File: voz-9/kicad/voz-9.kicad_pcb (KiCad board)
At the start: 2 copper layers, 300 x 140 mm, 189 parts, among them J1 OSC, J2 LFO, J3 DELAY, J4 PATCH A, J5 PATCH B, J6 CTRL, J7 IN+PRE, J8 OUT, J9 EQ424, Q1 J201, Q2 J201, Q3 J201, Q4 J201, Q5 J201, Q6 J201, Q7 2N5457, U1 NE5532, U2 TL072, U3 TL072, U4 MAX1044, U5 78M05, U6 PT2399, U7 PT2399, U8 PT2399, U9 TL072

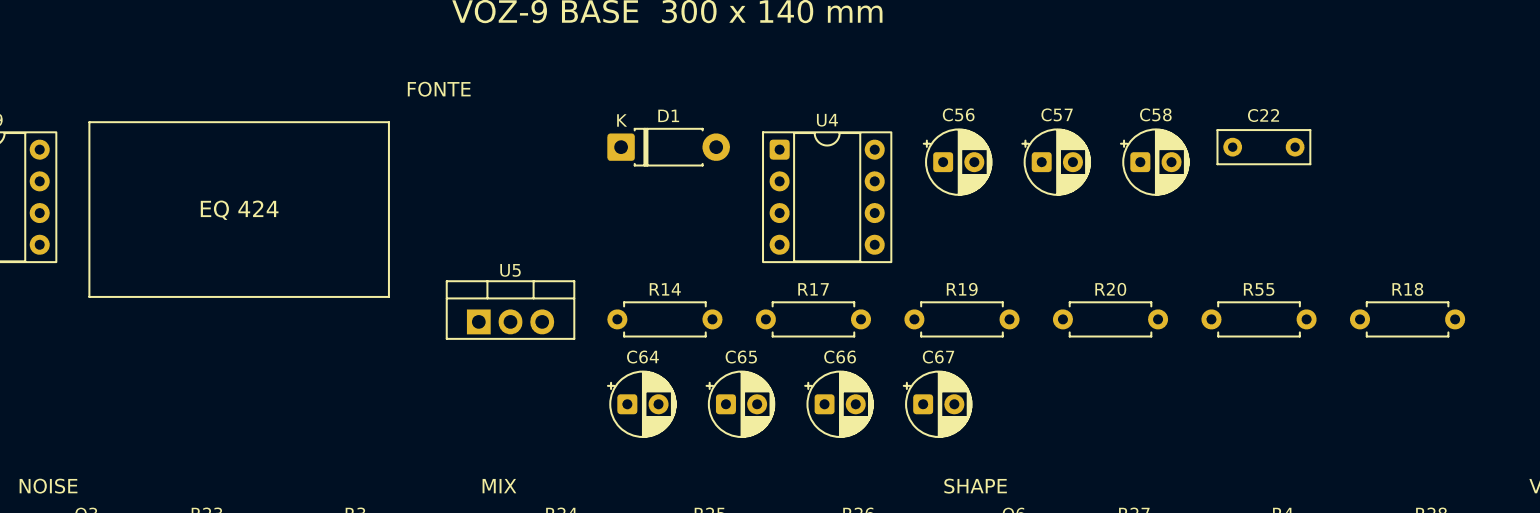
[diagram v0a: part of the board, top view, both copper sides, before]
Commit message: Tira a baía vazia do EQ na seda e encosta a fonte no U9.
O retângulo EQ 424 só reservava espaço em branco ao lado do TL072. A fonte sobe para x=106 mm, sem a caixa na seda.

Co-authored-by: Andrey <andreysenes@users.noreply.github.com>
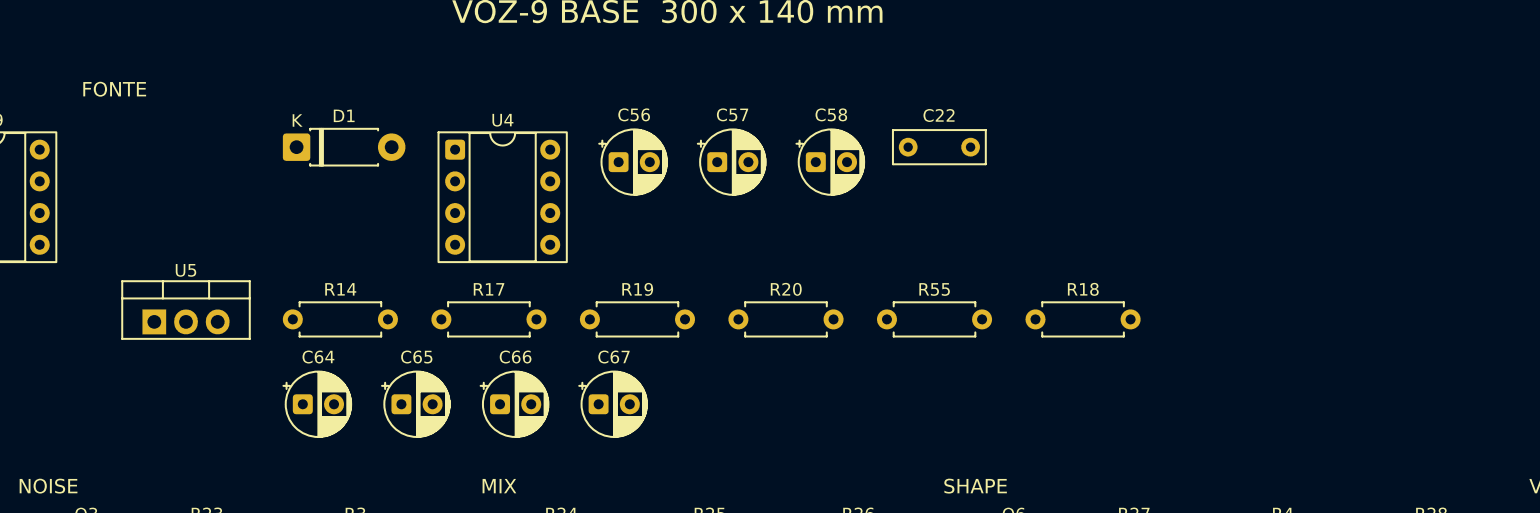
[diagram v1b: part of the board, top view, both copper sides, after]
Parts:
- moved C64 26.0 mm to (120.7, 36.6)
- moved D1 26.0 mm to (120.2, 16.0)
- moved R14 26.0 mm to (119.9, 29.8)
- moved C22 26.0 mm to (169.2, 16.0)
- moved C56 26.0 mm to (146.0, 17.2)
- moved C57 26.0 mm to (153.9, 17.2)
- moved C58 26.0 mm to (161.8, 17.2)
- moved C65 26.0 mm to (128.6, 36.6)
- moved C66 26.0 mm to (136.5, 36.6)
- moved C67 26.0 mm to (144.4, 36.6)
- moved R17 26.0 mm to (131.8, 29.8)
- moved R18 26.0 mm to (179.4, 29.8)
- moved R19 26.0 mm to (143.7, 29.8)
- moved R20 26.0 mm to (155.6, 29.8)
- moved R55 26.0 mm to (167.5, 29.8)
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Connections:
- C1 pad 1: XLR_HOT -> (no net)
- C1 pad 2: GND -> (no net)
- C10 pad 1: U6_LP1 -> (no net)
- C10 pad 2: GND -> (no net)
- C11 pad 1: U7_LP1 -> (no net)
- C11 pad 2: GND -> (no net)
- C12 pad 1: U8_LP1 -> (no net)
- C12 pad 2: GND -> (no net)
- C13 pad 1: U6_OP -> (no net)
- C13 pad 2: U6_OUT -> (no net)
- C14 pad 1: U7_OP -> (no net)
- C14 pad 2: U7_OUT -> (no net)
- C15 pad 1: U8_OP -> (no net)
- C15 pad 2: U8_OUT -> (no net)
- C16 pad 1: U6_LP1 -> (no net)
- C16 pad 2: GND -> (no net)
- C17 pad 1: U7_LP1 -> (no net)
- C17 pad 2: GND -> (no net)
- C18 pad 1: U8_LP1 -> (no net)
- C18 pad 2: GND -> (no net)
- C19 pad 1: V9 -> (no net)
- C19 pad 2: GND -> (no net)
- C2 pad 1: XLR_COLD -> (no net)
- C2 pad 2: GND -> (no net)
- C20 pad 1: U3A_OUT -> (no net)
- C20 pad 2: HEADS -> (no net)
- C21 pad 1: U2A_INM -> (no net)
- C21 pad 2: N4V5 -> (no net)
- C22 pad 1: V5 -> (no net)
- C22 pad 2: GND -> (no net)
- C23 pad 1: V9 -> (no net)
- C23 pad 2: GND -> (no net)
- C24 pad 1: VEE -> (no net)
- C24 pad 2: GND -> (no net)
- C25 pad 1: U1_OA -> (no net)
- C25 pad 2: U1_BP -> (no net)
- C26 pad 1: NOISE_D -> (no net)
- C26 pad 2: NOISE_MIX -> (no net)
- C27 pad 1: PRE_W -> (no net)
- C27 pad 2: FALA -> (no net)
- C28 pad 1: SHAPE -> (no net)
- C28 pad 2: FILT_SW -> (no net)
- C29 pad 1: WET_MIX -> (no net)
- C29 pad 2: LE_IN -> (no net)
- C3 pad 1: WET_LP -> (no net)
- C3 pad 2: GND -> (no net)
- C30 pad 1: MIX -> (no net)
- C30 pad 2: EQ_IN -> (no net)
- C31 pad 1: V5 -> (no net)
- C31 pad 2: GND -> (no net)
- C32 pad 1: V5 -> (no net)
- C32 pad 2: GND -> (no net)
- C33 pad 1: V5 -> (no net)
- C33 pad 2: GND -> (no net)
- C34 pad 1: U6_OUT -> (no net)
- C34 pad 2: U6_SW -> (no net)
- C35 pad 1: U7_OUT -> (no net)
- C35 pad 2: U7_SW -> (no net)
- C36 pad 1: U8_OUT -> (no net)
- C36 pad 2: U8_SW -> (no net)
- C37 pad 1: PT_REF_U6 -> (no net)
- C37 pad 2: GND -> (no net)
- C38 pad 1: PT_REF_U7 -> (no net)
- C38 pad 2: GND -> (no net)
- C39 pad 1: PT_REF_U8 -> (no net)
- C39 pad 2: GND -> (no net)
- C4 pad 1: U3A_IN -> (no net)
- C4 pad 2: U3A_OUT -> (no net)
- C40 pad 1: V9 -> (no net)
- C40 pad 2: GND -> (no net)
- C41 pad 1: PRE_W -> (no net)
- C41 pad 2: OSCIN_CW -> (no net)
- C42 pad 1: U1_OB -> (no net)
- C42 pad 2: PRE_CW -> (no net)
- C43 pad 1: LFO_D -> (no net)
- C43 pad 2: LFO_N1 -> (no net)
- C44 pad 1: LFO_N1 -> (no net)
- C44 pad 2: LFO_N2 -> (no net)
- C45 pad 1: INST_TIP -> (no net)
- C45 pad 2: EXT_IN -> (no net)
- C46 pad 1: TREM_A -> (no net)
- C46 pad 2: LFO_G -> (no net)
- C47 pad 1: VCF -> (no net)
- C47 pad 2: GND -> (no net)
- C48 pad 1: GRAVA_IN -> (no net)
- C48 pad 2: NAB_MID -> (no net)
- C49 pad 1: NAB_BASS -> (no net)
- C49 pad 2: WET -> (no net)
- C5 pad 1: U3B_IN -> (no net)
- C5 pad 2: WET -> (no net)
- C50 pad 1: VCF -> (no net)
- C50 pad 2: VCA_D -> (no net)
- C51 pad 1: U2A_OUT -> (no net)
- C51 pad 2: SW_A -> (no net)
- C52 pad 1: U2B_OUT -> (no net)
- C52 pad 2: SW_B -> (no net)
- C53 pad 1: LFO_D -> (no net)
- C53 pad 2: LFO_AC -> (no net)
- C54 pad 1: VCA_S -> (no net)
- C54 pad 2: DRY -> (no net)
- C55 pad 1: CLK_B -> (no net)
- C55 pad 2: GND -> (no net)
- C56 pad 1: U4_CAP+ -> (no net)
- C56 pad 2: U4_CAP- -> (no net)
- C57 pad 1: VEE -> (no net)
- C57 pad 2: GND -> (no net)
- C58 pad 1: V5 -> (no net)
- C58 pad 2: GND -> (no net)
- C59 pad 1: XLR_HOT -> (no net)
- C59 pad 2: PRE_R12 -> (no net)
- C6 pad 1: U2B_INM -> (no net)
- C6 pad 2: N4V5 -> (no net)
- C60 pad 1: XLR_COLD -> (no net)
- C60 pad 2: PRE_R13 -> (no net)
- C61 pad 1: V9 -> (no net)
- C61 pad 2: GND -> (no net)
- C62 pad 1: VEE -> (no net)
- C62 pad 2: GND -> (no net)
- C63 pad 1: V5 -> (no net)
- C63 pad 2: GND -> (no net)
- C64 pad 1: V9 -> (no net)
- C64 pad 2: GND -> (no net)
- C65 pad 1: VEE -> (no net)
- C65 pad 2: GND -> (no net)
- C66 pad 1: N4V5 -> (no net)
- C66 pad 2: GND -> (no net)
- C67 pad 1: N1V8 -> (no net)
- C67 pad 2: GND -> (no net)
- C68 pad 1: ENV -> (no net)
- C68 pad 2: GND -> (no net)
- C69 pad 1: U7_OUT -> (no net)
- C69 pad 2: U7_SW -> (no net)
- C7 pad 1: U6_CC1 -> (no net)
- C7 pad 2: U6_CC0 -> (no net)
- C70 pad 1: U8_OUT -> (no net)
- C70 pad 2: U8_SW -> (no net)
- C71 pad 1: TREM_B -> (no net)
- C71 pad 2: LFO_G -> (no net)
- C8 pad 1: U7_CC1 -> (no net)
- C8 pad 2: U7_CC0 -> (no net)
- C9 pad 1: U8_CC1 -> (no net)
- C9 pad 2: U8_CC0 -> (no net)
- D1 pad 1: V9 -> (no net)
- D1 pad 2: P4_TIP -> (no net)
- D2 pad 1: ENV -> (no net)
- D2 pad 2: GATE -> (no net)
- D3 pad 1: ENV -> (no net)
- D3 pad 2: FALA_A -> (no net)
- D4 pad 1: CLK_B -> (no net)
- D4 pad 2: CLK_A -> (no net)
- D6 pad 1: GND -> (no net)
- D6 pad 2: SHAPE -> (no net)
- D7 pad 1: GND -> (no net)
- D7 pad 2: WET -> (no net)
- J1 pad 1: OSC_A_POT -> (no net)
- J1 pad 10: GND -> (no net)
- J1 pad 11: N1V8 -> (no net)
- J1 pad 12: CUT_W -> (no net)
- J1 pad 13: GND -> (no net)
- J1 pad 14: SW_A -> (no net)
- J1 pad 15: SW_A_ON -> (no net)
- J1 pad 16: SW_B -> (no net)
- J1 pad 17: SW_B_ON -> (no net)
- J1 pad 18: N1V8 -> (no net)
- J1 pad 19: ENV -> (no net)
- J1 pad 2: U2A_INM -> (no net)
- J1 pad 3: OSC_B_POT -> (no net)
- J1 pad 4: U2B_INM -> (no net)
- J1 pad 5: SUM -> (no net)
- J1 pad 6: AMT_W -> (no net)
- J1 pad 7: GND -> (no net)
- J1 pad 8: EQ_OUT -> (no net)
- J1 pad 9: SHAPE_W -> (no net)
- J2 pad 1: RATE_W -> (no net)
- J2 pad 10: DEPTH_W -> (no net)
- J2 pad 11: PITCH_CV -> (no net)
- J2 pad 12: TIME_CV -> (no net)
- J2 pad 2: RATE_W -> (no net)
- J2 pad 3: GND -> (no net)
- J2 pad 4: LFO_OUT -> (no net)
- J2 pad 5: DEPTH_W -> (no net)
- J2 pad 6: GND -> (no net)
- J2 pad 7: LFO_N2 -> (no net)
- J2 pad 8: TREM_A -> (no net)
- J2 pad 9: TREM_B -> (no net)
- J3 pad 1: V5 -> (no net)
- J3 pad 10: GND -> (no net)
- J3 pad 11: STAR -> (no net)
- J3 pad 12: FB_CW -> (no net)
- J3 pad 13: DRY -> (no net)
- J3 pad 14: WET_W -> (no net)
- J3 pad 15: WET -> (no net)
- J3 pad 16: U6_SW -> (no net)
- J3 pad 17: U7_IN -> (no net)
- J3 pad 18: GND -> (no net)
- J3 pad 19: OUT -> (no net)
- J3 pad 2: TIME_W -> (no net)
- J3 pad 20: WET_W -> (no net)
- J3 pad 3: GND -> (no net)
- J3 pad 4: U6_SW -> (no net)
- J3 pad 5: H1_ON -> (no net)
- J3 pad 6: U7_SW -> (no net)
- J3 pad 7: H2_ON -> (no net)
- J3 pad 8: U8_SW -> (no net)
- J3 pad 9: H3_ON -> (no net)
- J4 pad 1: SW_A_ON -> (no net)
- J4 pad 10: FILT_TIP -> (no net)
- J4 pad 11: FILT_SW -> (no net)
- J4 pad 12: GND -> (no net)
- J4 pad 13: FCV -> (no net)
- J4 pad 15: GND -> (no net)
- J4 pad 16: VCV -> (no net)
- J4 pad 18: GND -> (no net)
- J4 pad 3: GND -> (no net)
- J4 pad 4: SW_B_ON -> (no net)
- J4 pad 6: GND -> (no net)
- J4 pad 7: EXT_IN -> (no net)
- J4 pad 9: GND -> (no net)
- J5 pad 1: LFO_OUT -> (no net)
- J5 pad 10: PRE_W -> (no net)
- J5 pad 12: GND -> (no net)
- J5 pad 13: STAR -> (no net)
- J5 pad 14: PRE_W -> (no net)
- J5 pad 15: GND -> (no net)
- J5 pad 3: GND -> (no net)
- J5 pad 4: TIME_CV -> (no net)
- J5 pad 6: GND -> (no net)
- J5 pad 7: CLK_TIP -> (no net)
- J5 pad 9: GND -> (no net)
- J6 pad 1: LED_A -> (no net)
- J6 pad 2: GND -> (no net)
- J6 pad 3: P4_TIP -> (no net)
- J6 pad 4: GND -> (no net)
- J6 pad 5: GATE -> (no net)
- J6 pad 6: GND -> (no net)
- J7 pad 1: XLR_HOT -> (no net)
- J7 pad 10: MIX -> (no net)
- J7 pad 11: OSCIN_CW -> (no net)
- J7 pad 2: XLR_COLD -> (no net)
- J7 pad 3: GND -> (no net)
- J7 pad 4: INST_TIP -> (no net)
- J7 pad 5: GND -> (no net)
- J7 pad 6: GND -> (no net)
- J7 pad 7: PRE_W -> (no net)
- J7 pad 8: PRE_CW -> (no net)
- J7 pad 9: AMT_W -> (no net)
- J8 pad 1: XLR_OUT -> (no net)
- J8 pad 2: J8_COLD -> (no net)
- J8 pad 3: GND -> (no net)
- J8 pad 4: OUT -> (no net)
- J8 pad 5: GND -> (no net)
- Q1 pad 1: U2A_INM -> (no net)
- Q1 pad 2: Q1G -> (no net)
- Q1 pad 3: N4V5 -> (no net)
- Q2 pad 1: U2B_INM -> (no net)
- Q2 pad 2: Q2G -> (no net)
- Q2 pad 3: N4V5 -> (no net)
- Q3 pad 1: NOISE_D -> (no net)
- Q3 pad 2: Q3G -> (no net)
- Q3 pad 3: NOISE_S -> (no net)
- Q4 pad 1: VCF -> (no net)
- Q4 pad 2: Q4G -> (no net)
- Q4 pad 3: N1V8 -> (no net)
- Q5 pad 1: VCA_D -> (no net)
- Q5 pad 2: ENV -> (no net)
- Q5 pad 3: VCA_S -> (no net)
- Q6 pad 1: V9 -> (no net)
- Q6 pad 2: Q6G -> (no net)
- Q6 pad 3: Q6S -> (no net)
- Q7 pad 1: LFO_D -> (no net)
- Q7 pad 2: LFO_G -> (no net)
- Q7 pad 3: LFO_S -> (no net)
- R1 pad 1: XLR_OUT -> (no net)
- R1 pad 2: GND -> (no net)
- R10 pad 1: H3A -> (no net)
- R10 pad 2: H3B -> (no net)
- R11 pad 1: TIME_W -> (no net)
- R11 pad 2: PT6_U6 -> (no net)
- R12 pad 1: PRE_R12 -> (no net)
- R12 pad 2: U1_INP -> (no net)
- R13 pad 1: PRE_R13 -> (no net)
- R13 pad 2: U1_INM -> (no net)
- R14 pad 1: V9 -> (no net)
- R14 pad 2: LED_A -> (no net)
- R15 pad 1: LFO_G -> (no net)
- R15 pad 2: RATE_W -> (no net)
- R16 pad 1: NAB_MID -> (no net)
- R16 pad 2: U3A_IN -> (no net)
- R18 pad 1: N1V8 -> (no net)
- R18 pad 2: GND -> (no net)
- R19 pad 1: V9 -> (no net)
- R19 pad 2: N4V5 -> (no net)
- R2 pad 1: J8_COLD -> (no net)
- R2 pad 2: GND -> (no net)
- R20 pad 1: N4V5 -> (no net)
- R20 pad 2: GND -> (no net)
- R21 pad 1: U2A_OUT -> (no net)
- R21 pad 2: OSC_A_POT -> (no net)
- R22 pad 1: U2B_OUT -> (no net)
- R22 pad 2: OSC_B_POT -> (no net)
- R23 pad 1: V9 -> (no net)
- R23 pad 2: NOISE_D -> (no net)
- R24 pad 1: SW_A_ON -> (no net)
- R24 pad 2: SUM -> (no net)
- R25 pad 1: SW_B_ON -> (no net)
- R25 pad 2: SUM -> (no net)
- R26 pad 1: EXT_IN -> (no net)
- R26 pad 2: SUM -> (no net)
- R27 pad 1: EQ_OUT -> (no net)
- R27 pad 2: Q6G -> (no net)
- R28 pad 1: Q6S -> (no net)
- R28 pad 2: SHAPE -> (no net)
- R29 pad 1: SHAPE_W -> (no net)
- R29 pad 2: SHAPE -> (no net)
- R3 pad 1: NOISE_S -> (no net)
- R3 pad 2: GND -> (no net)
- R30 pad 1: FILT_TIP -> (no net)
- R30 pad 2: VCF -> (no net)
- R31 pad 1: V9 -> (no net)
- R31 pad 2: LFO_D -> (no net)
- R32 pad 1: LFO_N1 -> (no net)
- R32 pad 2: GND -> (no net)
- R33 pad 1: LFO_N2 -> (no net)
- R33 pad 2: GND -> (no net)
- R34 pad 1: VCA_S -> (no net)
- R34 pad 2: N1V8 -> (no net)
- R35 pad 1: HEADS -> (no net)
- R35 pad 2: U6_IN -> (no net)
- R36 pad 1: HEADS -> (no net)
- R36 pad 2: U7_IN -> (no net)
- R37 pad 1: HEADS -> (no net)
- R37 pad 2: U8_IN -> (no net)
- R38 pad 1: H1_ON -> (no net)
- R38 pad 2: WET_MIX -> (no net)
- R39 pad 1: H2_ON -> (no net)
- R39 pad 2: WET_MIX -> (no net)
- R4 pad 1: Q6S -> (no net)
- R4 pad 2: N4V5 -> (no net)
- R40 pad 1: H3_ON -> (no net)
- R40 pad 2: WET_MIX -> (no net)
- R41 pad 1: U6_IN -> (no net)
- R41 pad 2: U6_LP1 -> (no net)
- R42 pad 1: U1_BM -> (no net)
- R42 pad 2: U1_OB -> (no net)
- R43 pad 1: CLK_A -> (no net)
- R43 pad 2: GND -> (no net)
- R44 pad 1: OUT -> (no net)
- R44 pad 2: XLR_OUT -> (no net)
- R45 pad 1: U3B_IN -> (no net)
- R45 pad 2: NAB_BASS -> (no net)
- R46 pad 1: DRY -> (no net)
- R46 pad 2: STAR -> (no net)
- R47 pad 1: U7_IN -> (no net)
- R47 pad 2: U7_LP1 -> (no net)
- R48 pad 1: U8_IN -> (no net)
- R48 pad 2: U8_LP1 -> (no net)
- R49 pad 1: WET -> (no net)
- R49 pad 2: WET_LP -> (no net)
- R5 pad 1: LFO_S -> (no net)
- R5 pad 2: GND -> (no net)
- R50 pad 1: FALA -> (no net)
- R50 pad 2: FALA_A -> (no net)
- R51 pad 1: STAR -> (no net)
- R51 pad 2: GRAVA_IN -> (no net)
- R52 pad 1: U3A_IN -> (no net)
- R52 pad 2: U3A_OUT -> (no net)
- R53 pad 1: LE_IN -> (no net)
- R53 pad 2: U3B_IN -> (no net)
- R54 pad 1: U3B_IN -> (no net)
- R54 pad 2: WET -> (no net)
- R55 pad 1: V9 -> (no net)
- R55 pad 2: N1V8 -> (no net)
- R56 pad 1: H2B -> (no net)
- R56 pad 2: PT6_U7 -> (no net)
- R57 pad 1: U1_INM -> (no net)
- R57 pad 2: U1_OA -> (no net)
- R58 pad 1: U1_INP -> (no net)
- R58 pad 2: GND -> (no net)
- R59 pad 1: CLK_TIP -> (no net)
- R59 pad 2: CLK_A -> (no net)
- R6 pad 1: U1_BM -> (no net)
- R6 pad 2: GND -> (no net)
- R60 pad 1: H3B -> (no net)
- R60 pad 2: PT6_U8 -> (no net)
- R61 pad 1: VCF -> (no net)
- R61 pad 2: RES_W -> (no net)
- R62 pad 1: U2A_OUT -> (no net)
- R62 pad 2: U2A_INP -> (no net)
- R63 pad 1: U2A_INP -> (no net)
- R63 pad 2: N4V5 -> (no net)
- R64 pad 1: NOISE_MIX -> (no net)
- R64 pad 2: SUM -> (no net)
- R65 pad 1: PITCH_CV -> (no net)
- R65 pad 2: Q1G -> (no net)
- R66 pad 1: PITCH_CV -> (no net)
- R66 pad 2: Q2G -> (no net)
- R67 pad 1: Q4G -> (no net)
- R67 pad 2: FCV -> (no net)
- R68 pad 1: CUT_W -> (no net)
- R68 pad 2: Q4G -> (no net)
- R69 pad 1: ENV -> (no net)
- R69 pad 2: VCV -> (no net)
- R7 pad 1: TIME_W -> (no net)
- R7 pad 2: H2A -> (no net)
- R70 pad 1: CLK_B -> (no net)
- R70 pad 2: TIME_CV -> (no net)
- R71 pad 1: WET -> (no net)
- R71 pad 2: WET_W -> (no net)
- R72 pad 1: U2B_OUT -> (no net)
- R72 pad 2: U2B_INP -> (no net)
- R73 pad 1: U2B_INP -> (no net)
- R73 pad 2: N4V5 -> (no net)
- R74 pad 1: ENV -> (no net)
- R74 pad 2: GND -> (no net)
- R75 pad 1: TIME_CV -> (no net)
- R75 pad 2: PT6_U6 -> (no net)
- R76 pad 1: TIME_CV -> (no net)
- R76 pad 2: PT6_U7 -> (no net)
- R77 pad 1: TIME_CV -> (no net)
- R77 pad 2: PT6_U8 -> (no net)
- R78 pad 1: CLK_B -> (no net)
- R78 pad 2: GND -> (no net)
- R79 pad 1: LFO_AC -> (no net)
- R79 pad 2: LFO_OUT -> (no net)
- R8 pad 1: H2A -> (no net)
- R8 pad 2: H2B -> (no net)
- R80 pad 1: Q3G -> (no net)
- R80 pad 2: GND -> (no net)
- R81 pad 1: LFO_G -> (no net)
- R81 pad 2: GND -> (no net)
- R9 pad 1: TIME_W -> (no net)
- R9 pad 2: H3A -> (no net)
- RV1 pad 1: WET -> (no net)
- RV1 pad 2: FB_CW -> (no net)
- RV1 pad 3: FB_CW -> (no net)
- RV2 pad 1: FILT_TIP -> (no net)
- RV2 pad 2: RES_W -> (no net)
- RV2 pad 3: FILT_TIP -> (no net)
- U1 pad 1: U1_OA -> (no net)
- U1 pad 2: U1_INM -> (no net)
- U1 pad 3: U1_INP -> (no net)
- U1 pad 4: VEE -> (no net)
- U1 pad 5: U1_BP -> (no net)
- U1 pad 6: U1_BM -> (no net)
- U1 pad 7: U1_OB -> (no net)
- U1 pad 8: V9 -> (no net)
- U2 pad 1: U2A_OUT -> (no net)
- U2 pad 2: U2A_INM -> (no net)
- U2 pad 3: U2A_INP -> (no net)
- U2 pad 4: GND -> (no net)
- U2 pad 5: U2B_INP -> (no net)
- U2 pad 6: U2B_INM -> (no net)
- U2 pad 7: U2B_OUT -> (no net)
- U2 pad 8: V9 -> (no net)
- U3 pad 1: U3A_OUT -> (no net)
- U3 pad 2: U3A_IN -> (no net)
- U3 pad 3: GND -> (no net)
- U3 pad 4: VEE -> (no net)
- U3 pad 5: GND -> (no net)
- U3 pad 6: U3B_IN -> (no net)
- U3 pad 7: WET -> (no net)
- U3 pad 8: V9 -> (no net)
- U4 pad 2: U4_CAP+ -> (no net)
- U4 pad 3: GND -> (no net)
- U4 pad 4: U4_CAP- -> (no net)
- U4 pad 5: VEE -> (no net)
- U4 pad 8: V9 -> (no net)
- U5 pad 1: V9 -> (no net)
- U5 pad 2: GND -> (no net)
- U5 pad 3: V5 -> (no net)
- U6 pad 1: V5 -> (no net)
- U6 pad 10: U6_OP -> (no net)
- U6 pad 11: U6_OP -> (no net)
- U6 pad 12: U6_OP -> (no net)
- U6 pad 13: U6_OP -> (no net)
- U6 pad 14: U6_OUT -> (no net)
- U6 pad 15: U6_LP1 -> (no net)
- U6 pad 16: U6_IN -> (no net)
- U6 pad 2: PT_REF_U6 -> (no net)
- U6 pad 3: GND -> (no net)
- U6 pad 4: GND -> (no net)
- U6 pad 6: PT6_U6 -> (no net)
- U6 pad 7: U6_CC1 -> (no net)
- U6 pad 8: U6_CC0 -> (no net)
- U6 pad 9: U6_OP -> (no net)
- U7 pad 1: V5 -> (no net)
- U7 pad 10: U7_OP -> (no net)
- U7 pad 11: U7_OP -> (no net)
- U7 pad 12: U7_OP -> (no net)
- U7 pad 13: U7_OP -> (no net)
- U7 pad 14: U7_OUT -> (no net)
- U7 pad 15: U7_LP1 -> (no net)
- U7 pad 16: U7_IN -> (no net)
- U7 pad 2: PT_REF_U7 -> (no net)
- U7 pad 3: GND -> (no net)
- U7 pad 4: GND -> (no net)
- U7 pad 6: PT6_U7 -> (no net)
- U7 pad 7: U7_CC1 -> (no net)
- U7 pad 8: U7_CC0 -> (no net)
- U7 pad 9: U7_OP -> (no net)
- U8 pad 1: V5 -> (no net)
- U8 pad 10: U8_OP -> (no net)
- U8 pad 11: U8_OP -> (no net)
- U8 pad 12: U8_OP -> (no net)
- U8 pad 13: U8_OP -> (no net)
- U8 pad 14: U8_OUT -> (no net)
- U8 pad 15: U8_LP1 -> (no net)
- U8 pad 16: U8_IN -> (no net)
- U8 pad 2: PT_REF_U8 -> (no net)
- U8 pad 3: GND -> (no net)
- U8 pad 4: GND -> (no net)
- U8 pad 6: PT6_U8 -> (no net)
- U8 pad 7: U8_CC1 -> (no net)
- U8 pad 8: U8_CC0 -> (no net)
- U8 pad 9: U8_OP -> (no net)
- U9 pad 1: EQ_A -> (no net)
- U9 pad 2: EQ_A -> (no net)
- U9 pad 3: EQ_IN -> (no net)
- U9 pad 4: VEE -> (no net)
- U9 pad 5: EQ_A -> (no net)
- U9 pad 6: EQ_OUT -> (no net)
- U9 pad 7: EQ_OUT -> (no net)
- U9 pad 8: V9 -> (no net)
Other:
- board text removed: "EQ 424"

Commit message: Roteia a BASE de 300×140 mm e fecha o H1_ON.
O autorroteador deixou o pino 5 do J3 aberto e dois furos 0,006 mm perto demais. O fechamento agora desvia de pino sem net e de furo, e o DRC fica sem erro e sem pad solto.

Co-authored-by: Andrey <andreysenes@users.noreply.github.com>
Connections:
- C1 pad 1: (no net) -> XLR_HOT
- C1 pad 2: (no net) -> GND
- C10 pad 1: (no net) -> U6_LP1
- C10 pad 2: (no net) -> GND
- C11 pad 1: (no net) -> U7_LP1
- C11 pad 2: (no net) -> GND
- C12 pad 1: (no net) -> U8_LP1
- C12 pad 2: (no net) -> GND
- C13 pad 1: (no net) -> U6_OP
- C13 pad 2: (no net) -> U6_OUT
- C14 pad 1: (no net) -> U7_OP
- C14 pad 2: (no net) -> U7_OUT
- C15 pad 1: (no net) -> U8_OP
- C15 pad 2: (no net) -> U8_OUT
- C16 pad 1: (no net) -> U6_LP1
- C16 pad 2: (no net) -> GND
- C17 pad 1: (no net) -> U7_LP1
- C17 pad 2: (no net) -> GND
- C18 pad 1: (no net) -> U8_LP1
- C18 pad 2: (no net) -> GND
- C19 pad 1: (no net) -> V9
- C19 pad 2: (no net) -> GND
- C2 pad 1: (no net) -> XLR_COLD
- C2 pad 2: (no net) -> GND
- C20 pad 1: (no net) -> U3A_OUT
- C20 pad 2: (no net) -> HEADS
- C21 pad 1: (no net) -> U2A_INM
- C21 pad 2: (no net) -> N4V5
- C22 pad 1: (no net) -> V5
- C22 pad 2: (no net) -> GND
- C23 pad 1: (no net) -> V9
- C23 pad 2: (no net) -> GND
- C24 pad 1: (no net) -> VEE
- C24 pad 2: (no net) -> GND
- C25 pad 1: (no net) -> U1_OA
- C25 pad 2: (no net) -> U1_BP
- C26 pad 1: (no net) -> NOISE_D
- C26 pad 2: (no net) -> NOISE_MIX
- C27 pad 1: (no net) -> PRE_W
- C27 pad 2: (no net) -> FALA
- C28 pad 1: (no net) -> SHAPE
- C28 pad 2: (no net) -> FILT_SW
- C29 pad 1: (no net) -> WET_MIX
- C29 pad 2: (no net) -> LE_IN
- C3 pad 1: (no net) -> WET_LP
- C3 pad 2: (no net) -> GND
- C30 pad 1: (no net) -> MIX
- C30 pad 2: (no net) -> EQ_IN
- C31 pad 1: (no net) -> V5
- C31 pad 2: (no net) -> GND
- C32 pad 1: (no net) -> V5
- C32 pad 2: (no net) -> GND
- C33 pad 1: (no net) -> V5
- C33 pad 2: (no net) -> GND
- C34 pad 1: (no net) -> U6_OUT
- C34 pad 2: (no net) -> U6_SW
- C35 pad 1: (no net) -> U7_OUT
- C35 pad 2: (no net) -> U7_SW
- C36 pad 1: (no net) -> U8_OUT
- C36 pad 2: (no net) -> U8_SW
- C37 pad 1: (no net) -> PT_REF_U6
- C37 pad 2: (no net) -> GND
- C38 pad 1: (no net) -> PT_REF_U7
- C38 pad 2: (no net) -> GND
- C39 pad 1: (no net) -> PT_REF_U8
- C39 pad 2: (no net) -> GND
- C4 pad 1: (no net) -> U3A_IN
- C4 pad 2: (no net) -> U3A_OUT
- C40 pad 1: (no net) -> V9
- C40 pad 2: (no net) -> GND
- C41 pad 1: (no net) -> PRE_W
- C41 pad 2: (no net) -> OSCIN_CW
- C42 pad 1: (no net) -> U1_OB
- C42 pad 2: (no net) -> PRE_CW
- C43 pad 1: (no net) -> LFO_D
- C43 pad 2: (no net) -> LFO_N1
- C44 pad 1: (no net) -> LFO_N1
- C44 pad 2: (no net) -> LFO_N2
- C45 pad 1: (no net) -> INST_TIP
- C45 pad 2: (no net) -> EXT_IN
- C46 pad 1: (no net) -> TREM_A
- C46 pad 2: (no net) -> LFO_G
- C47 pad 1: (no net) -> VCF
- C47 pad 2: (no net) -> GND
- C48 pad 1: (no net) -> GRAVA_IN
- C48 pad 2: (no net) -> NAB_MID
- C49 pad 1: (no net) -> NAB_BASS
- C49 pad 2: (no net) -> WET
- C5 pad 1: (no net) -> U3B_IN
- C5 pad 2: (no net) -> WET
- C50 pad 1: (no net) -> VCF
- C50 pad 2: (no net) -> VCA_D
- C51 pad 1: (no net) -> U2A_OUT
- C51 pad 2: (no net) -> SW_A
- C52 pad 1: (no net) -> U2B_OUT
- C52 pad 2: (no net) -> SW_B
- C53 pad 1: (no net) -> LFO_D
- C53 pad 2: (no net) -> LFO_AC
- C54 pad 1: (no net) -> VCA_S
- C54 pad 2: (no net) -> DRY
- C55 pad 1: (no net) -> CLK_B
- C55 pad 2: (no net) -> GND
- C56 pad 1: (no net) -> U4_CAP+
- C56 pad 2: (no net) -> U4_CAP-
- C57 pad 1: (no net) -> VEE
- C57 pad 2: (no net) -> GND
- C58 pad 1: (no net) -> V5
- C58 pad 2: (no net) -> GND
- C59 pad 1: (no net) -> XLR_HOT
- C59 pad 2: (no net) -> PRE_R12
- C6 pad 1: (no net) -> U2B_INM
- C6 pad 2: (no net) -> N4V5
- C60 pad 1: (no net) -> XLR_COLD
- C60 pad 2: (no net) -> PRE_R13
- C61 pad 1: (no net) -> V9
- C61 pad 2: (no net) -> GND
- C62 pad 1: (no net) -> VEE
- C62 pad 2: (no net) -> GND
- C63 pad 1: (no net) -> V5
- C63 pad 2: (no net) -> GND
- C64 pad 1: (no net) -> V9
- C64 pad 2: (no net) -> GND
- C65 pad 1: (no net) -> VEE
- C65 pad 2: (no net) -> GND
- C66 pad 1: (no net) -> N4V5
- C66 pad 2: (no net) -> GND
- C67 pad 1: (no net) -> N1V8
- C67 pad 2: (no net) -> GND
- C68 pad 1: (no net) -> ENV
- C68 pad 2: (no net) -> GND
- C69 pad 1: (no net) -> U7_OUT
- C69 pad 2: (no net) -> U7_SW
- C7 pad 1: (no net) -> U6_CC1
- C7 pad 2: (no net) -> U6_CC0
- C70 pad 1: (no net) -> U8_OUT
- C70 pad 2: (no net) -> U8_SW
- C71 pad 1: (no net) -> TREM_B
- C71 pad 2: (no net) -> LFO_G
- C8 pad 1: (no net) -> U7_CC1
- C8 pad 2: (no net) -> U7_CC0
- C9 pad 1: (no net) -> U8_CC1
- C9 pad 2: (no net) -> U8_CC0
- D1 pad 1: (no net) -> V9
- D1 pad 2: (no net) -> P4_TIP
- D2 pad 1: (no net) -> ENV
- D2 pad 2: (no net) -> GATE
- D3 pad 1: (no net) -> ENV
- D3 pad 2: (no net) -> FALA_A
- D4 pad 1: (no net) -> CLK_B
- D4 pad 2: (no net) -> CLK_A
- D6 pad 1: (no net) -> GND
- D6 pad 2: (no net) -> SHAPE
- D7 pad 1: (no net) -> GND
- D7 pad 2: (no net) -> WET
- J1 pad 1: (no net) -> OSC_A_POT
- J1 pad 10: (no net) -> GND
- J1 pad 11: (no net) -> N1V8
- J1 pad 12: (no net) -> CUT_W
- J1 pad 13: (no net) -> GND
- J1 pad 14: (no net) -> SW_A
- J1 pad 15: (no net) -> SW_A_ON
- J1 pad 16: (no net) -> SW_B
- J1 pad 17: (no net) -> SW_B_ON
- J1 pad 18: (no net) -> N1V8
- J1 pad 19: (no net) -> ENV
- J1 pad 2: (no net) -> U2A_INM
- J1 pad 3: (no net) -> OSC_B_POT
- J1 pad 4: (no net) -> U2B_INM
- J1 pad 5: (no net) -> SUM
- J1 pad 6: (no net) -> AMT_W
- J1 pad 7: (no net) -> GND
- J1 pad 8: (no net) -> EQ_OUT
- J1 pad 9: (no net) -> SHAPE_W
- J2 pad 1: (no net) -> RATE_W
- J2 pad 10: (no net) -> DEPTH_W
- J2 pad 11: (no net) -> PITCH_CV
- J2 pad 12: (no net) -> TIME_CV
- J2 pad 2: (no net) -> RATE_W
- J2 pad 3: (no net) -> GND
- J2 pad 4: (no net) -> LFO_OUT
- J2 pad 5: (no net) -> DEPTH_W
- J2 pad 6: (no net) -> GND
- J2 pad 7: (no net) -> LFO_N2
- J2 pad 8: (no net) -> TREM_A
- J2 pad 9: (no net) -> TREM_B
- J3 pad 1: (no net) -> V5
- J3 pad 10: (no net) -> GND
- J3 pad 11: (no net) -> STAR
- J3 pad 12: (no net) -> FB_CW
- J3 pad 13: (no net) -> DRY
- J3 pad 14: (no net) -> WET_W
- J3 pad 15: (no net) -> WET
- J3 pad 16: (no net) -> U6_SW
- J3 pad 17: (no net) -> U7_IN
- J3 pad 18: (no net) -> GND
- J3 pad 19: (no net) -> OUT
- J3 pad 2: (no net) -> TIME_W
- J3 pad 20: (no net) -> WET_W
- J3 pad 3: (no net) -> GND
- J3 pad 4: (no net) -> U6_SW
- J3 pad 5: (no net) -> H1_ON
- J3 pad 6: (no net) -> U7_SW
- J3 pad 7: (no net) -> H2_ON
- J3 pad 8: (no net) -> U8_SW
- J3 pad 9: (no net) -> H3_ON
- J4 pad 1: (no net) -> SW_A_ON
- J4 pad 10: (no net) -> FILT_TIP
- J4 pad 11: (no net) -> FILT_SW
- J4 pad 12: (no net) -> GND
- J4 pad 13: (no net) -> FCV
- J4 pad 15: (no net) -> GND
- J4 pad 16: (no net) -> VCV
- J4 pad 18: (no net) -> GND
- J4 pad 3: (no net) -> GND
- J4 pad 4: (no net) -> SW_B_ON
- J4 pad 6: (no net) -> GND
- J4 pad 7: (no net) -> EXT_IN
- J4 pad 9: (no net) -> GND
- J5 pad 1: (no net) -> LFO_OUT
- J5 pad 10: (no net) -> PRE_W
- J5 pad 12: (no net) -> GND
- J5 pad 13: (no net) -> STAR
- J5 pad 14: (no net) -> PRE_W
- J5 pad 15: (no net) -> GND
- J5 pad 3: (no net) -> GND
- J5 pad 4: (no net) -> TIME_CV
- J5 pad 6: (no net) -> GND
- J5 pad 7: (no net) -> CLK_TIP
- J5 pad 9: (no net) -> GND
- J6 pad 1: (no net) -> LED_A
- J6 pad 2: (no net) -> GND
- J6 pad 3: (no net) -> P4_TIP
- J6 pad 4: (no net) -> GND
- J6 pad 5: (no net) -> GATE
- J6 pad 6: (no net) -> GND
- J7 pad 1: (no net) -> XLR_HOT
- J7 pad 10: (no net) -> MIX
- J7 pad 11: (no net) -> OSCIN_CW
- J7 pad 2: (no net) -> XLR_COLD
- J7 pad 3: (no net) -> GND
- J7 pad 4: (no net) -> INST_TIP
- J7 pad 5: (no net) -> GND
- J7 pad 6: (no net) -> GND
- J7 pad 7: (no net) -> PRE_W
- J7 pad 8: (no net) -> PRE_CW
- J7 pad 9: (no net) -> AMT_W
- J8 pad 1: (no net) -> XLR_OUT
- J8 pad 2: (no net) -> J8_COLD
- J8 pad 3: (no net) -> GND
- J8 pad 4: (no net) -> OUT
- J8 pad 5: (no net) -> GND
- Q1 pad 1: (no net) -> U2A_INM
- Q1 pad 2: (no net) -> Q1G
- Q1 pad 3: (no net) -> N4V5
- Q2 pad 1: (no net) -> U2B_INM
- Q2 pad 2: (no net) -> Q2G
- Q2 pad 3: (no net) -> N4V5
- Q3 pad 1: (no net) -> NOISE_D
- Q3 pad 2: (no net) -> Q3G
- Q3 pad 3: (no net) -> NOISE_S
- Q4 pad 1: (no net) -> VCF
- Q4 pad 2: (no net) -> Q4G
- Q4 pad 3: (no net) -> N1V8
- Q5 pad 1: (no net) -> VCA_D
- Q5 pad 2: (no net) -> ENV
- Q5 pad 3: (no net) -> VCA_S
- Q6 pad 1: (no net) -> V9
- Q6 pad 2: (no net) -> Q6G
- Q6 pad 3: (no net) -> Q6S
- Q7 pad 1: (no net) -> LFO_D
- Q7 pad 2: (no net) -> LFO_G
- Q7 pad 3: (no net) -> LFO_S
- R1 pad 1: (no net) -> XLR_OUT
- R1 pad 2: (no net) -> GND
- R10 pad 1: (no net) -> H3A
- R10 pad 2: (no net) -> H3B
- R11 pad 1: (no net) -> TIME_W
- R11 pad 2: (no net) -> PT6_U6
- R12 pad 1: (no net) -> PRE_R12
- R12 pad 2: (no net) -> U1_INP
- R13 pad 1: (no net) -> PRE_R13
- R13 pad 2: (no net) -> U1_INM
- R14 pad 1: (no net) -> V9
- R14 pad 2: (no net) -> LED_A
- R15 pad 1: (no net) -> LFO_G
- R15 pad 2: (no net) -> RATE_W
- R16 pad 1: (no net) -> NAB_MID
- R16 pad 2: (no net) -> U3A_IN
- R18 pad 1: (no net) -> N1V8
- R18 pad 2: (no net) -> GND
- R19 pad 1: (no net) -> V9
- R19 pad 2: (no net) -> N4V5
- R2 pad 1: (no net) -> J8_COLD
- R2 pad 2: (no net) -> GND
- R20 pad 1: (no net) -> N4V5
- R20 pad 2: (no net) -> GND
- R21 pad 1: (no net) -> U2A_OUT
- R21 pad 2: (no net) -> OSC_A_POT
- R22 pad 1: (no net) -> U2B_OUT
- R22 pad 2: (no net) -> OSC_B_POT
- R23 pad 1: (no net) -> V9
- R23 pad 2: (no net) -> NOISE_D
- R24 pad 1: (no net) -> SW_A_ON
- R24 pad 2: (no net) -> SUM
- R25 pad 1: (no net) -> SW_B_ON
- R25 pad 2: (no net) -> SUM
- R26 pad 1: (no net) -> EXT_IN
- R26 pad 2: (no net) -> SUM
- R27 pad 1: (no net) -> EQ_OUT
- R27 pad 2: (no net) -> Q6G
- R28 pad 1: (no net) -> Q6S
- R28 pad 2: (no net) -> SHAPE
- R29 pad 1: (no net) -> SHAPE_W
- R29 pad 2: (no net) -> SHAPE
- R3 pad 1: (no net) -> NOISE_S
- R3 pad 2: (no net) -> GND
- R30 pad 1: (no net) -> FILT_TIP
- R30 pad 2: (no net) -> VCF
- R31 pad 1: (no net) -> V9
- R31 pad 2: (no net) -> LFO_D
- R32 pad 1: (no net) -> LFO_N1
- R32 pad 2: (no net) -> GND
- R33 pad 1: (no net) -> LFO_N2
- R33 pad 2: (no net) -> GND
- R34 pad 1: (no net) -> VCA_S
- R34 pad 2: (no net) -> N1V8
- R35 pad 1: (no net) -> HEADS
- R35 pad 2: (no net) -> U6_IN
- R36 pad 1: (no net) -> HEADS
- R36 pad 2: (no net) -> U7_IN
- R37 pad 1: (no net) -> HEADS
- R37 pad 2: (no net) -> U8_IN
- R38 pad 1: (no net) -> H1_ON
- R38 pad 2: (no net) -> WET_MIX
- R39 pad 1: (no net) -> H2_ON
- R39 pad 2: (no net) -> WET_MIX
- R4 pad 1: (no net) -> Q6S
- R4 pad 2: (no net) -> N4V5
- R40 pad 1: (no net) -> H3_ON
- R40 pad 2: (no net) -> WET_MIX
- R41 pad 1: (no net) -> U6_IN
- R41 pad 2: (no net) -> U6_LP1
- R42 pad 1: (no net) -> U1_BM
- R42 pad 2: (no net) -> U1_OB
- R43 pad 1: (no net) -> CLK_A
- R43 pad 2: (no net) -> GND
- R44 pad 1: (no net) -> OUT
- R44 pad 2: (no net) -> XLR_OUT
- R45 pad 1: (no net) -> U3B_IN
- R45 pad 2: (no net) -> NAB_BASS
- R46 pad 1: (no net) -> DRY
- R46 pad 2: (no net) -> STAR
- R47 pad 1: (no net) -> U7_IN
- R47 pad 2: (no net) -> U7_LP1
- R48 pad 1: (no net) -> U8_IN
- R48 pad 2: (no net) -> U8_LP1
- R49 pad 1: (no net) -> WET
- R49 pad 2: (no net) -> WET_LP
- R5 pad 1: (no net) -> LFO_S
- R5 pad 2: (no net) -> GND
- R50 pad 1: (no net) -> FALA
- R50 pad 2: (no net) -> FALA_A
- R51 pad 1: (no net) -> STAR
- R51 pad 2: (no net) -> GRAVA_IN
- R52 pad 1: (no net) -> U3A_IN
- R52 pad 2: (no net) -> U3A_OUT
- R53 pad 1: (no net) -> LE_IN
- R53 pad 2: (no net) -> U3B_IN
- R54 pad 1: (no net) -> U3B_IN
- R54 pad 2: (no net) -> WET
- R55 pad 1: (no net) -> V9
- R55 pad 2: (no net) -> N1V8
- R56 pad 1: (no net) -> H2B
- R56 pad 2: (no net) -> PT6_U7
- R57 pad 1: (no net) -> U1_INM
- R57 pad 2: (no net) -> U1_OA
- R58 pad 1: (no net) -> U1_INP
- R58 pad 2: (no net) -> GND
- R59 pad 1: (no net) -> CLK_TIP
- R59 pad 2: (no net) -> CLK_A
- R6 pad 1: (no net) -> U1_BM
- R6 pad 2: (no net) -> GND
- R60 pad 1: (no net) -> H3B
- R60 pad 2: (no net) -> PT6_U8
- R61 pad 1: (no net) -> VCF
- R61 pad 2: (no net) -> RES_W
- R62 pad 1: (no net) -> U2A_OUT
- R62 pad 2: (no net) -> U2A_INP
- R63 pad 1: (no net) -> U2A_INP
- R63 pad 2: (no net) -> N4V5
- R64 pad 1: (no net) -> NOISE_MIX
- R64 pad 2: (no net) -> SUM
- R65 pad 1: (no net) -> PITCH_CV
- R65 pad 2: (no net) -> Q1G
- R66 pad 1: (no net) -> PITCH_CV
- R66 pad 2: (no net) -> Q2G
- R67 pad 1: (no net) -> Q4G
- R67 pad 2: (no net) -> FCV
- R68 pad 1: (no net) -> CUT_W
- R68 pad 2: (no net) -> Q4G
- R69 pad 1: (no net) -> ENV
- R69 pad 2: (no net) -> VCV
- R7 pad 1: (no net) -> TIME_W
- R7 pad 2: (no net) -> H2A
- R70 pad 1: (no net) -> CLK_B
- R70 pad 2: (no net) -> TIME_CV
- R71 pad 1: (no net) -> WET
- R71 pad 2: (no net) -> WET_W
- R72 pad 1: (no net) -> U2B_OUT
- R72 pad 2: (no net) -> U2B_INP
- R73 pad 1: (no net) -> U2B_INP
- R73 pad 2: (no net) -> N4V5
- R74 pad 1: (no net) -> ENV
- R74 pad 2: (no net) -> GND
- R75 pad 1: (no net) -> TIME_CV
- R75 pad 2: (no net) -> PT6_U6
- R76 pad 1: (no net) -> TIME_CV
- R76 pad 2: (no net) -> PT6_U7
- R77 pad 1: (no net) -> TIME_CV
- R77 pad 2: (no net) -> PT6_U8
- R78 pad 1: (no net) -> CLK_B
- R78 pad 2: (no net) -> GND
- R79 pad 1: (no net) -> LFO_AC
- R79 pad 2: (no net) -> LFO_OUT
- R8 pad 1: (no net) -> H2A
- R8 pad 2: (no net) -> H2B
- R80 pad 1: (no net) -> Q3G
- R80 pad 2: (no net) -> GND
- R81 pad 1: (no net) -> LFO_G
- R81 pad 2: (no net) -> GND
- R9 pad 1: (no net) -> TIME_W
- R9 pad 2: (no net) -> H3A
- RV1 pad 1: (no net) -> WET
- RV1 pad 2: (no net) -> FB_CW
- RV1 pad 3: (no net) -> FB_CW
- RV2 pad 1: (no net) -> FILT_TIP
- RV2 pad 2: (no net) -> RES_W
- RV2 pad 3: (no net) -> FILT_TIP
- U1 pad 1: (no net) -> U1_OA
- U1 pad 2: (no net) -> U1_INM
- U1 pad 3: (no net) -> U1_INP
- U1 pad 4: (no net) -> VEE
- U1 pad 5: (no net) -> U1_BP
- U1 pad 6: (no net) -> U1_BM
- U1 pad 7: (no net) -> U1_OB
- U1 pad 8: (no net) -> V9
- U2 pad 1: (no net) -> U2A_OUT
- U2 pad 2: (no net) -> U2A_INM
- U2 pad 3: (no net) -> U2A_INP
- U2 pad 4: (no net) -> GND
- U2 pad 5: (no net) -> U2B_INP
- U2 pad 6: (no net) -> U2B_INM
- U2 pad 7: (no net) -> U2B_OUT
- U2 pad 8: (no net) -> V9
- U3 pad 1: (no net) -> U3A_OUT
- U3 pad 2: (no net) -> U3A_IN
- U3 pad 3: (no net) -> GND
- U3 pad 4: (no net) -> VEE
- U3 pad 5: (no net) -> GND
- U3 pad 6: (no net) -> U3B_IN
- U3 pad 7: (no net) -> WET
- U3 pad 8: (no net) -> V9
- U4 pad 2: (no net) -> U4_CAP+
- U4 pad 3: (no net) -> GND
- U4 pad 4: (no net) -> U4_CAP-
- U4 pad 5: (no net) -> VEE
- U4 pad 8: (no net) -> V9
- U5 pad 1: (no net) -> V9
- U5 pad 2: (no net) -> GND
- U5 pad 3: (no net) -> V5
- U6 pad 1: (no net) -> V5
- U6 pad 10: (no net) -> U6_OP
- U6 pad 11: (no net) -> U6_OP
- U6 pad 12: (no net) -> U6_OP
- U6 pad 13: (no net) -> U6_OP
- U6 pad 14: (no net) -> U6_OUT
- U6 pad 15: (no net) -> U6_LP1
- U6 pad 16: (no net) -> U6_IN
- U6 pad 2: (no net) -> PT_REF_U6
- U6 pad 3: (no net) -> GND
- U6 pad 4: (no net) -> GND
- U6 pad 6: (no net) -> PT6_U6
- U6 pad 7: (no net) -> U6_CC1
- U6 pad 8: (no net) -> U6_CC0
- U6 pad 9: (no net) -> U6_OP
- U7 pad 1: (no net) -> V5
- U7 pad 10: (no net) -> U7_OP
- U7 pad 11: (no net) -> U7_OP
- U7 pad 12: (no net) -> U7_OP
- U7 pad 13: (no net) -> U7_OP
- U7 pad 14: (no net) -> U7_OUT
- U7 pad 15: (no net) -> U7_LP1
- U7 pad 16: (no net) -> U7_IN
- U7 pad 2: (no net) -> PT_REF_U7
- U7 pad 3: (no net) -> GND
- U7 pad 4: (no net) -> GND
- U7 pad 6: (no net) -> PT6_U7
- U7 pad 7: (no net) -> U7_CC1
- U7 pad 8: (no net) -> U7_CC0
- U7 pad 9: (no net) -> U7_OP
- U8 pad 1: (no net) -> V5
- U8 pad 10: (no net) -> U8_OP
- U8 pad 11: (no net) -> U8_OP
- U8 pad 12: (no net) -> U8_OP
- U8 pad 13: (no net) -> U8_OP
- U8 pad 14: (no net) -> U8_OUT
- U8 pad 15: (no net) -> U8_LP1
- U8 pad 16: (no net) -> U8_IN
- U8 pad 2: (no net) -> PT_REF_U8
- U8 pad 3: (no net) -> GND
- U8 pad 4: (no net) -> GND
- U8 pad 6: (no net) -> PT6_U8
- U8 pad 7: (no net) -> U8_CC1
- U8 pad 8: (no net) -> U8_CC0
- U8 pad 9: (no net) -> U8_OP
- U9 pad 1: (no net) -> EQ_A
- U9 pad 2: (no net) -> EQ_A
- U9 pad 3: (no net) -> EQ_IN
- U9 pad 4: (no net) -> VEE
- U9 pad 5: (no net) -> EQ_A
- U9 pad 6: (no net) -> EQ_OUT
- U9 pad 7: (no net) -> EQ_OUT
- U9 pad 8: (no net) -> V9
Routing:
- net GND: track 0.00 -> 1337.1 mm
- net PRE_W: track 0.00 -> 432.8 mm, vias 0 -> 3
- net V5: track 0.00 -> 429.8 mm
- net WET: track 0.00 -> 380.9 mm, vias 0 -> 2
- net TIME_CV: track 0.00 -> 367.3 mm, vias 0 -> 5
- net V9: track 0.00 -> 346.8 mm
- net N1V8: track 0.00 -> 329.7 mm, vias 0 -> 3
- net H1_ON: track 0.00 -> 316.1 mm, vias 0 -> 15
- net STAR: track 0.00 -> 297.8 mm, vias 0 -> 3
- net LFO_OUT: track 0.00 -> 293.8 mm
- net CUT_W: track 0.00 -> 292.0 mm, vias 0 -> 3
- net DRY: track 0.00 -> 291.3 mm, vias 0 -> 6
- net VEE: track 0.00 -> 283.7 mm, vias 0 -> 1
- net SUM: track 0.00 -> 262.7 mm, vias 0 -> 1
- net ENV: track 0.00 -> 253.2 mm, vias 0 -> 1
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- added copper zone on B.Cu, net GND

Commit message: Troca o título da seda por v.1.
O texto VOZ-9 BASE 300 x 140 mm saiu do topo da placa. A revisão da folha acompanha.

Co-authored-by: Andrey <andreysenes@users.noreply.github.com>
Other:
- board text added: "v.1"
- board text removed: "VOZ-9 BASE 300 x 140 mm"
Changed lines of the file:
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@@
 		(title "VOZ-9 BASE")
 		(date "2026-09-27")
-		(rev "A")
+		(rev "v.1")
 		(comment 1 "300 x 140 mm")
 		(comment 2 "Blocos junto do conector. Duas placas cabem numa chapa de 300 x 300.")
@@
 		)
 	)
-	(gr_text "VOZ-9 BASE  300 x 140 mm"
+	(gr_text "v.1"
 		(at 150 5.2 0)
 		(layer "F.SilkS")

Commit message: Liga o EQ 424, o GATE e a trava do CLK como a documentação pede.
O botão GATE fica em série entre 1V8 e o ânodo do 1N4148. U9 deixa de ser
um seguidor vazio: LOW, MID e HIGH entram em J9. AMOUNT, SHAPE e DEPTH
crescem no sentido horário. R71 passa a 10 k e D5 segura o CLK em 9 V.

Co-authored-by: Andrey <andreysenes@users.noreply.github.com>
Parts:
- added C72: 100n, Capacitor_THT:C_Rect_L7.2mm_W2.5mm_P5.00mm, F.Cu at (104.6, 21.6)
- added C73: 33n, Capacitor_THT:C_Rect_L7.2mm_W2.5mm_P5.00mm, F.Cu at (114.4, 21.6)
- added C74: 1n, Capacitor_THT:C_Rect_L7.2mm_W2.5mm_P5.00mm, F.Cu at (124.2, 21.6)
- added C75: 10n, Capacitor_THT:C_Rect_L7.2mm_W2.5mm_P5.00mm, F.Cu at (134.0, 21.6)
- added D5: 1N4148, Diode_THT:D_DO-41_SOD81_P7.62mm_Horizontal, F.Cu at (170.7, 107.3)
- added R82: 10k, Resistor_THT:R_Axial_DIN0207_L6.3mm_D2.5mm_P7.62mm_Horizontal, F.Cu at (104.3, 16.0)
- added R83: 10k, Resistor_THT:R_Axial_DIN0207_L6.3mm_D2.5mm_P7.62mm_Horizontal, F.Cu at (116.2, 16.0)
- added R84: 10k, Resistor_THT:R_Axial_DIN0207_L6.3mm_D2.5mm_P7.62mm_Horizontal, F.Cu at (128.1, 16.0)
- added R85: 100k, Resistor_THT:R_Axial_DIN0207_L6.3mm_D2.5mm_P7.62mm_Horizontal, F.Cu at (140.0, 16.0)
- added R86: 3k3, Resistor_THT:R_Axial_DIN0207_L6.3mm_D2.5mm_P7.62mm_Horizontal, F.Cu at (151.9, 16.0)
- R71: value 100k -> 10k
- moved U5 59.5 mm to (168.3, 30.0)
- moved C22 59.5 mm to (228.7, 16.0)
- moved C56 59.5 mm to (205.5, 17.2)
- moved C57 59.5 mm to (213.4, 17.2)
- moved C58 59.5 mm to (221.3, 17.2)
- moved C65 59.5 mm to (188.1, 36.6)
- moved C66 59.5 mm to (196.0, 36.6)
- moved C67 59.5 mm to (203.9, 36.6)
- moved R14 59.5 mm to (179.4, 29.8)
- moved R17 59.5 mm to (191.3, 29.8)
- moved R18 59.5 mm to (238.9, 29.8)
- moved R19 59.5 mm to (203.2, 29.8)
- moved R20 59.5 mm to (215.1, 29.8)
- moved R55 59.5 mm to (227.0, 29.8)
- moved U4 59.5 mm to (192.4, 16.2)
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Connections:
- J1 pad 10: GND -> EQ_OUT
- J1 pad 5: SUM -> GND
- J1 pad 7: GND -> SUM
- J1 pad 8: EQ_OUT -> GND
- J2 pad 4: LFO_OUT -> GND
- J2 pad 6: GND -> LFO_OUT
- J6 pad 5: GATE -> N1V8
- J6 pad 6: GND -> GATE
- J9 pad 1: (no net) -> EQ_BUF
- J9 pad 10: (no net) -> EQ_BUF
- J9 pad 11: (no net) -> HIGH_W
- J9 pad 12: (no net) -> EQ_B
- J9 pad 2: (no net) -> LOW_W
- J9 pad 3: (no net) -> EQ_B
- J9 pad 4: (no net) -> MIDF_W
- J9 pad 5: (no net) -> MIDF_W
- J9 pad 6: (no net) -> MIDF_CW
- J9 pad 7: (no net) -> EQ_BUF
- J9 pad 8: (no net) -> MIDG_W
- J9 pad 9: (no net) -> EQ_B
- U9 pad 1: EQ_A -> EQ_BUF
- U9 pad 2: EQ_A -> EQ_BUF
- U9 pad 5: EQ_A -> GND
- U9 pad 6: EQ_OUT -> EQ_SUM
- U9 pad 7: EQ_OUT -> EQ_B
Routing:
- net MIDF_W: track 0.00 -> 282.6 mm, vias 0 -> 6
- net EQ_B: track 0.00 -> 181.1 mm
- net HIGH_W: track 0.00 -> 180.0 mm, vias 0 -> 8
- net EQ_BUF: track 0.00 -> 172.5 mm
- net V9: track 346.8 -> 517.3 mm, vias 0 -> 2
- net MIDF_CW: track 0.00 -> 150.8 mm, vias 0 -> 4
- net LOW_W: track 0.00 -> 126.5 mm
- net MIDG_W: track 0.00 -> 123.1 mm
- net XLR_HOT: track 235.2 -> 137.6 mm
- net SW_A_ON: track 228.6 -> 312.7 mm, vias 0 -> 2
- net EQ_SUM: track 0.00 -> 83.8 mm
- net PRE_W: track 432.8 -> 353.3 mm, vias 3 -> 2
- net GND: track 1337.1 -> 1395.0 mm, vias 0 -> 1
- net SW_B: track 147.1 -> 89.9 mm, vias 9 -> 0
- net CUT_W: track 292.0 -> 348.0 mm
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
